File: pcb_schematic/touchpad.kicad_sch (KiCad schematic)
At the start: 12 parts, among them U1 touchpad, U2 CD74HC4067M, U3 ProMicro

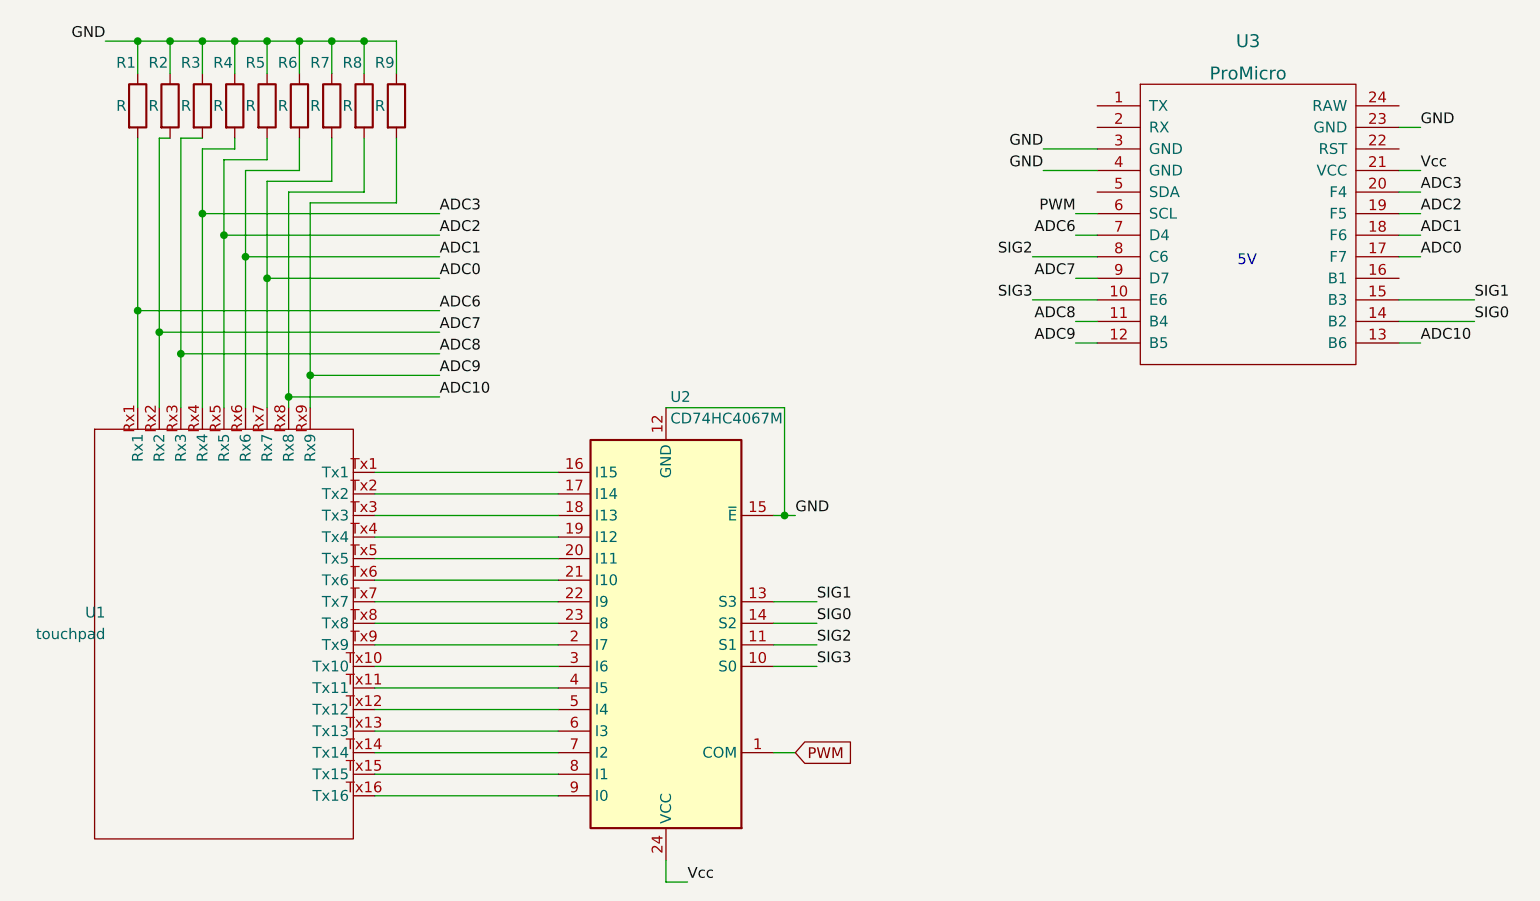
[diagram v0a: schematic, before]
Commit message: Fix PCB tag naming
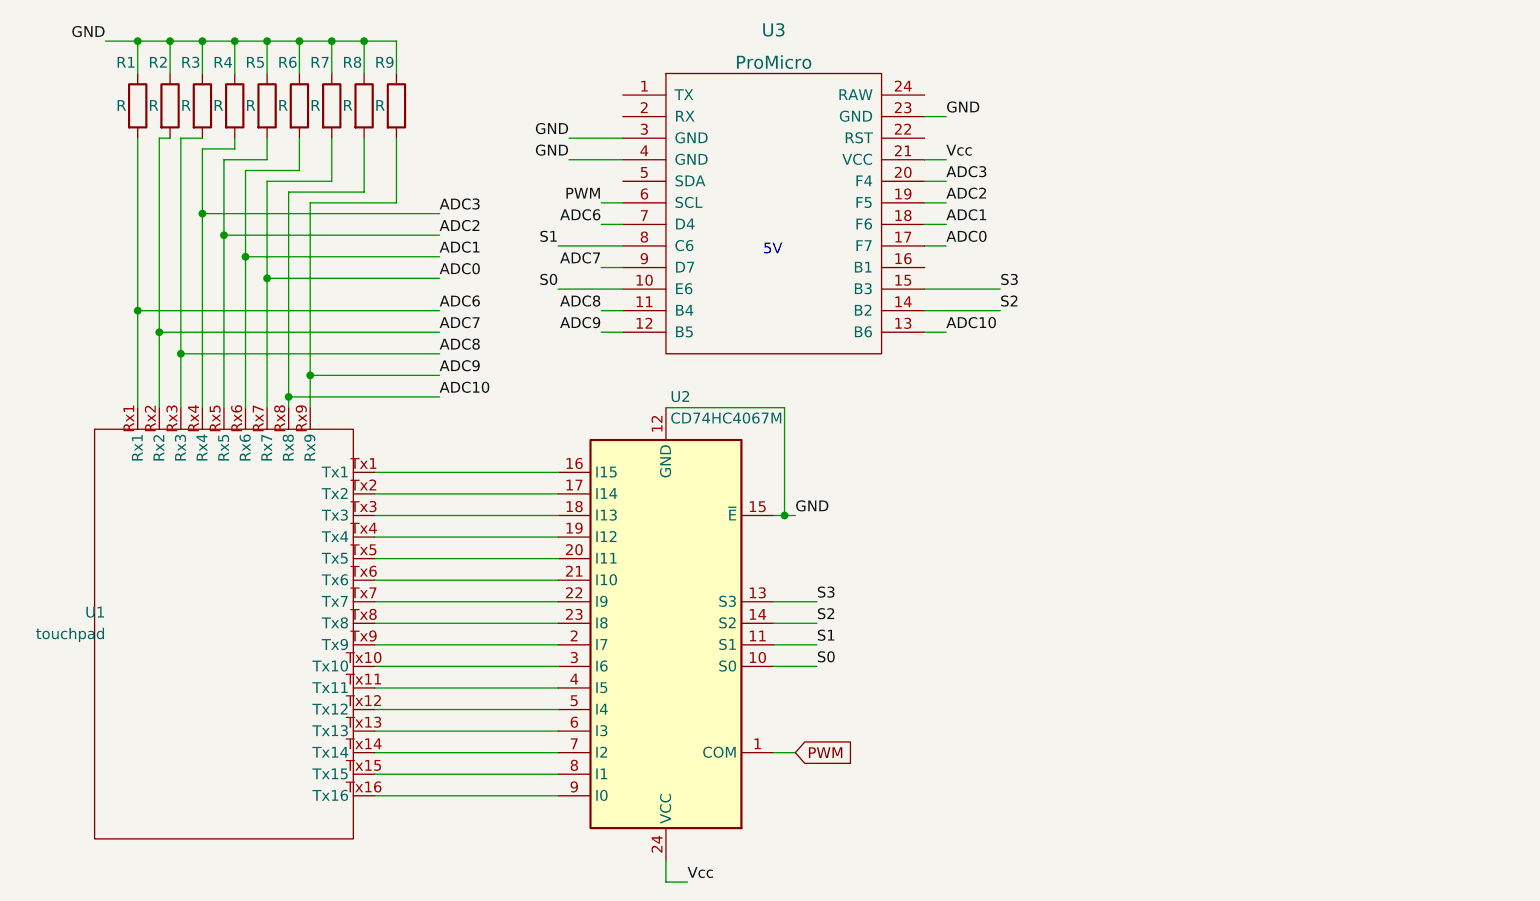
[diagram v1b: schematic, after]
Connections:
- net SIG0 renamed S2
- net SIG1 renamed S3
- net SIG2 renamed S1
- net SIG3 renamed S0
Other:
- moved on the sheet: U3
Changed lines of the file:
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@@
     (stroke (width 0) (type default) (color 0 0 0 0))
   )
-  (wire (pts (xy 147.32 52.07) (xy 149.86 52.07))
+  (wire (pts (xy 91.44 50.8) (xy 93.98 50.8))
     (stroke (width 0) (type default) (color 0 0 0 0))
   )
@@
     (stroke (width 0) (type default) (color 0 0 0 0))
   )
-  (wire (pts (xy 142.24 44.45) (xy 149.86 44.45))
+  (wire (pts (xy 86.36 43.18) (xy 93.98 43.18))
     (stroke (width 0) (type default) (color 0 0 0 0))
   )
@@
     (stroke (width 0) (type default) (color 0 0 0 0))
   )
-  (wire (pts (xy 185.42 49.53) (xy 194.31 49.53))
+  (wire (pts (xy 129.54 48.26) (xy 138.43 48.26))
     (stroke (width 0) (type default) (color 0 0 0 0))
   )
@@
     (stroke (width 0) (type default) (color 0 0 0 0))
   )
-  (wire (pts (xy 147.32 46.99) (xy 149.86 46.99))
+  (wire (pts (xy 91.44 45.72) (xy 93.98 45.72))
     (stroke (width 0) (type default) (color 0 0 0 0))
   )
@@
     (stroke (width 0) (type default) (color 0 0 0 0))
   )
-  (wire (pts (xy 147.32 54.61) (xy 149.86 54.61))
+  (wire (pts (xy 91.44 53.34) (xy 93.98 53.34))
     (stroke (width 0) (type default) (color 0 0 0 0))
   )
@@
     (stroke (width 0) (type default) (color 0 0 0 0))
   )
-  (wire (pts (xy 147.32 39.37) (xy 149.86 39.37))
+  (wire (pts (xy 91.44 38.1) (xy 93.98 38.1))
     (stroke (width 0) (type default) (color 0 0 0 0))
   )
@@
     (stroke (width 0) (type default) (color 0 0 0 0))
   )
-  (wire (pts (xy 143.51 31.75) (xy 149.86 31.75))
+  (wire (pts (xy 87.63 30.48) (xy 93.98 30.48))
     (stroke (width 0) (type default) (color 0 0 0 0))
   )
@@
     (stroke (width 0) (type default) (color 0 0 0 0))
   )
-  (wire (pts (xy 185.42 36.83) (xy 187.96 36.83))
+  (wire (pts (xy 129.54 35.56) (xy 132.08 35.56))
     (stroke (width 0) (type default) (color 0 0 0 0))
   )
@@
     (stroke (width 0) (type default) (color 0 0 0 0))
   )
-  (wire (pts (xy 185.42 29.21) (xy 187.96 29.21))
-    (stroke (width 0) (type default) (color 0 0 0 0))
-  )
-  (wire (pts (xy 143.51 34.29) (xy 149.86 34.29))
-    (stroke (width 0) (type default) (color 0 0 0 0))
-  )
-  (wire (pts (xy 185.42 54.61) (xy 187.96 54.61))
+  (wire (pts (xy 129.54 27.94) (xy 132.08 27.94))
+    (stroke (width 0) (type default) (color 0 0 0 0))
+  )
+  (wire (pts (xy 87.63 33.02) (xy 93.98 33.02))
+    (stroke (width 0) (type default) (color 0 0 0 0))
+  )
+  (wire (pts (xy 129.54 53.34) (xy 132.08 53.34))
     (stroke (width 0) (type default) (color 0 0 0 0))
   )
@@
     (stroke (width 0) (type default) (color 0 0 0 0))
   )
-  (wire (pts (xy 147.32 41.91) (xy 149.86 41.91))
+  (wire (pts (xy 91.44 40.64) (xy 93.98 40.64))
     (stroke (width 0) (type default) (color 0 0 0 0))
   )
@@
     (stroke (width 0) (type default) (color 0 0 0 0))
   )
-  (wire (pts (xy 185.42 41.91) (xy 187.96 41.91))
+  (wire (pts (xy 129.54 40.64) (xy 132.08 40.64))
     (stroke (width 0) (type default) (color 0 0 0 0))
   )
@@
     (stroke (width 0) (type default) (color 0 0 0 0))
   )
-  (wire (pts (xy 185.42 39.37) (xy 187.96 39.37))
-    (stroke (width 0) (type default) (color 0 0 0 0))
-  )
-  (wire (pts (xy 185.42 52.07) (xy 194.31 52.07))
+  (wire (pts (xy 129.54 38.1) (xy 132.08 38.1))
+    (stroke (width 0) (type default) (color 0 0 0 0))
+  )
+  (wire (pts (xy 129.54 50.8) (xy 138.43 50.8))
     (stroke (width 0) (type default) (color 0 0 0 0))
   )
@@
     (stroke (width 0) (type default) (color 0 0 0 0))
   )
-  (wire (pts (xy 185.42 44.45) (xy 187.96 44.45))
+  (wire (pts (xy 129.54 43.18) (xy 132.08 43.18))
     (stroke (width 0) (type default) (color 0 0 0 0))
   )
@@
     (stroke (width 0) (type default) (color 0 0 0 0))
   )
-  (wire (pts (xy 185.42 34.29) (xy 187.96 34.29))
+  (wire (pts (xy 129.54 33.02) (xy 132.08 33.02))
     (stroke (width 0) (type default) (color 0 0 0 0))
   )
@@
     (stroke (width 0) (type default) (color 0 0 0 0))
   )
-  (wire (pts (xy 142.24 49.53) (xy 149.86 49.53))
+  (wire (pts (xy 86.36 48.26) (xy 93.98 48.26))
     (stroke (width 0) (type default) (color 0 0 0 0))
   )
@@
     (stroke (width 0) (type default) (color 0 0 0 0))
   )
-  (text "5V" (at 166.37 45.72 0)
-    (effects (font (size 1.27 1.27)) (justify left bottom))
-  )
-  (label "SIG2" (at 142.24 44.45 180)
+  (text "5V" (at 110.49 44.45 0)
+    (effects (font (size 1.27 1.27)) (justify left bottom))
+  )
+  (label "S1" (at 86.36 43.18 180)
     (effects (font (size 1.27 1.27)) (justify right bottom))
   )
@@
     (effects (font (size 1.27 1.27)) (justify left bottom))
   )
-  (label "ADC6" (at 147.32 41.91 180)
-    (effects (font (size 1.27 1.27)) (justify right bottom))
-  )
-  (label "GND" (at 143.51 34.29 180)
-    (effects (font (size 1.27 1.27)) (justify right bottom))
-  )
-  (label "Vcc" (at 187.96 34.29 0)
-    (effects (font (size 1.27 1.27)) (justify left bottom))
-  )
-  (label "SIG3" (at 142.24 49.53 180)
-    (effects (font (size 1.27 1.27)) (justify right bottom))
-  )
-  (label "PWM" (at 147.32 39.37 180)
+  (label "ADC6" (at 91.44 40.64 180)
+    (effects (font (size 1.27 1.27)) (justify right bottom))
+  )
+  (label "GND" (at 87.63 33.02 180)
+    (effects (font (size 1.27 1.27)) (justify right bottom))
+  )
+  (label "Vcc" (at 132.08 33.02 0)
+    (effects (font (size 1.27 1.27)) (justify left bottom))
+  )
+  (label "S0" (at 86.36 48.26 180)
+    (effects (font (size 1.27 1.27)) (justify right bottom))
+  )
+  (label "PWM" (at 91.44 38.1 180)
     (effects (font (size 1.27 1.27)) (justify right bottom))
   )
@@
     (effects (font (size 1.27 1.27)) (justify left bottom))
   )
-  (label "SIG0" (at 116.84 87.63 0)
-    (effects (font (size 1.27 1.27)) (justify left bottom))
-  )
-  (label "ADC8" (at 147.32 52.07 180)
-    (effects (font (size 1.27 1.27)) (justify right bottom))
-  )
-  (label "SIG1" (at 116.84 85.09 0)
-    (effects (font (size 1.27 1.27)) (justify left bottom))
-  )
-  (label "ADC3" (at 187.96 36.83 0)
+  (label "S2" (at 116.84 87.63 0)
+    (effects (font (size 1.27 1.27)) (justify left bottom))
+  )
+  (label "ADC8" (at 91.44 50.8 180)
+    (effects (font (size 1.27 1.27)) (justify right bottom))
+  )
+  (label "S3" (at 116.84 85.09 0)
+    (effects (font (size 1.27 1.27)) (justify left bottom))
+  )
+  (label "ADC3" (at 132.08 35.56 0)
     (effects (font (size 1.27 1.27)) (justify left bottom))
   )
@@
     (effects (font (size 1.27 1.27)) (justify left bottom))
   )
-  (label "SIG0" (at 194.31 52.07 0)
+  (label "S2" (at 138.43 50.8 0)
     (effects (font (size 1.27 1.27)) (justify left bottom))
   )
@@
     (effects (font (size 1.27 1.27)) (justify left bottom))
   )
-  (label "ADC2" (at 187.96 39.37 0)
+  (label "ADC2" (at 132.08 38.1 0)
     (effects (font (size 1.27 1.27)) (justify left bottom))
   )
@@
     (effects (font (size 1.27 1.27)) (justify left bottom))
   )
-  (label "ADC10" (at 187.96 54.61 0)
-    (effects (font (size 1.27 1.27)) (justify left bottom))
-  )
-  (label "SIG3" (at 116.84 92.71 0)
+  (label "ADC10" (at 132.08 53.34 0)
+    (effects (font (size 1.27 1.27)) (justify left bottom))
+  )
+  (label "S0" (at 116.84 92.71 0)
     (effects (font (size 1.27 1.27)) (justify left bottom))
   )
@@
     (effects (font (size 1.27 1.27)) (justify right bottom))
   )
-  (label "ADC0" (at 187.96 44.45 0)
-    (effects (font (size 1.27 1.27)) (justify left bottom))
-  )
-  (label "GND" (at 143.51 31.75 180)
-    (effects (font (size 1.27 1.27)) (justify right bottom))
-  )
-  (label "ADC7" (at 147.32 46.99 180)
-    (effects (font (size 1.27 1.27)) (justify right bottom))
-  )
-  (label "SIG1" (at 194.31 49.53 0)
-    (effects (font (size 1.27 1.27)) (justify left bottom))
-  )
-  (label "ADC1" (at 187.96 41.91 0)
-    (effects (font (size 1.27 1.27)) (justify left bottom))
-  )
-  (label "SIG2" (at 116.84 90.17 0)
+  (label "ADC0" (at 132.08 43.18 0)
+    (effects (font (size 1.27 1.27)) (justify left bottom))
+  )
+  (label "GND" (at 87.63 30.48 180)
+    (effects (font (size 1.27 1.27)) (justify right bottom))
+  )
+  (label "ADC7" (at 91.44 45.72 180)
+    (effects (font (size 1.27 1.27)) (justify right bottom))
+  )
+  (label "S3" (at 138.43 48.26 0)
+    (effects (font (size 1.27 1.27)) (justify left bottom))
+  )
+  (label "ADC1" (at 132.08 40.64 0)
+    (effects (font (size 1.27 1.27)) (justify left bottom))
+  )
+  (label "S1" (at 116.84 90.17 0)
     (effects (font (size 1.27 1.27)) (justify left bottom))
   )
@@
     (effects (font (size 1.27 1.27)) (justify left bottom))
   )
-  (label "ADC9" (at 147.32 54.61 180)
+  (label "ADC9" (at 91.44 53.34 180)
     (effects (font (size 1.27 1.27)) (justify right bottom))
   )
@@
     (effects (font (size 1.27 1.27)) (justify left bottom))
   )
-  (label "GND" (at 187.96 29.21 0)
+  (label "GND" (at 132.08 27.94 0)
     (effects (font (size 1.27 1.27)) (justify left bottom))
   )
@@
   )
   (symbol (lib_id "74xx:CD74HC4067M") (at 99.06 90.17 180) (unit 1)
-    (in_bom yes) (on_board yes) (fields_autoplaced)
+    (in_bom yes) (on_board yes)
     (property "Reference" "U2" (id 0) (at 99.5806 60.96 0)
       (effects (font (size 1.27 1.27)) (justify right))
@@
     (pin "2")
   )
-  (symbol (lib_id "promicro:ProMicro") (at 167.64 45.72 0) (unit 1)
+  (symbol (lib_id "promicro:ProMicro") (at 111.76 44.45 0) (unit 1)
     (in_bom yes) (on_board yes) (fields_autoplaced)
-    (property "Reference" "U3" (id 0) (at 167.64 19.05 0)
+    (property "Reference" "U3" (id 0) (at 111.76 17.78 0)
       (effects (font (size 1.524 1.524)))
     )
-    (property "Value" "ProMicro" (id 1) (at 167.64 22.86 0)
+    (property "Value" "ProMicro" (id 1) (at 111.76 21.59 0)
       (effects (font (size 1.524 1.524)))
     )
-    (property "Footprint" "promicro:ProMicro" (id 2) (at 170.18 72.39 0)
+    (property "Footprint" "promicro:ProMicro" (id 2) (at 114.3 71.12 0)
       (effects (font (size 1.524 1.524)) hide)
     )
-    (property "Datasheet" "" (id 3) (at 170.18 72.39 0)
+    (property "Datasheet" "" (id 3) (at 114.3 71.12 0)
       (effects (font (size 1.524 1.524)))
     )

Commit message: Update PCB
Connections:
- net PWM: now also U3.8 (C6); no longer U3.6 (SCL)
- net S1: now also U3.14 (B2); no longer U3.8 (C6)
- net S2: now also U3.15 (B3); no longer U3.14 (B2)
- net S3: now also U3.16 (B1); no longer U3.15 (B3)
